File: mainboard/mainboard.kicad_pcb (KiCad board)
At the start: 2 copper layers, 344.7 x 96.3 mm, 5 parts

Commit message: grounding
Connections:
- A1 pad 100: /H2-48 -> GND
- A1 pad 61: /H2-9 -> GND
- A1 pad 66: /H2-14 -> GND
- A1 pad 69: /H2-17 -> GND
- A1 pad 73: /H2-21 -> GND
- A1 pad 74: /H2-22 -> GND
- A1 pad 81: /H2-29 -> GND
- A1 pad 82: /H2-30 -> GND
- A1 pad 84: /H2-32 -> GND
- A1 pad 99: /H2-47 -> GND
- A2 pad 100: /H2-48 -> GND
- A2 pad 61: /H2-9 -> GND
- A2 pad 66: /H2-14 -> GND
- A2 pad 69: /H2-17 -> GND
- A2 pad 73: /H2-21 -> GND
- A2 pad 74: /H2-22 -> GND
- A2 pad 81: /H2-29 -> GND
- A2 pad 82: /H2-30 -> GND
- A2 pad 84: /H2-32 -> GND
- A2 pad 99: /H2-47 -> GND
- A3 pad 100: /H2-48 -> GND
- A3 pad 61: /H2-9 -> GND
- A3 pad 66: /H2-14 -> GND
- A3 pad 69: /H2-17 -> GND
- A3 pad 73: /H2-21 -> GND
- A3 pad 74: /H2-22 -> GND
- A3 pad 81: /H2-29 -> GND
- A3 pad 82: /H2-30 -> GND
- A3 pad 84: /H2-32 -> GND
- A3 pad 99: /H2-47 -> GND
- A4 pad 100: /H2-48 -> GND
- A4 pad 61: /H2-9 -> GND
- A4 pad 66: /H2-14 -> GND
- A4 pad 69: /H2-17 -> GND
- A4 pad 73: /H2-21 -> GND
- A4 pad 74: /H2-22 -> GND
- A4 pad 81: /H2-29 -> GND
- A4 pad 82: /H2-30 -> GND
- A4 pad 84: /H2-32 -> GND
- A4 pad 99: /H2-47 -> GND
- A5 pad 100: /H2-48 -> GND
- A5 pad 61: /H2-9 -> GND
- A5 pad 66: /H2-14 -> GND
- A5 pad 69: /H2-17 -> GND
- A5 pad 73: /H2-21 -> GND
- A5 pad 74: /H2-22 -> GND
- A5 pad 81: /H2-29 -> GND
- A5 pad 82: /H2-30 -> GND
- A5 pad 84: /H2-32 -> GND
- A5 pad 99: /H2-47 -> GND
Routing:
- net GND: track 0.00 -> 159.0 mm
- net /H1-47: track 1.88 -> 86.9 mm
- net /H1-48: track 4.90 -> 87.1 mm, vias 0 -> 2
- net /H2-22: track 10.6 -> 0.00 mm
- net /H2-14: track 10.4 -> 0.00 mm
- net /H2-32: track 10.4 -> 0.00 mm
- net /H2-30: track 10.4 -> 0.00 mm
- net /H2-48: track 10.0 -> 0.00 mm
- net /H2-21: track 7.53 -> 0.00 mm
- net /H2-17: track 7.53 -> 0.00 mm
- net /H2-9: track 7.53 -> 0.00 mm
- net /H2-29: track 7.53 -> 0.00 mm
- net /H2-47: track 7.42 -> 0.00 mm

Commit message: bus power flags, finish left side routing
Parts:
- added H1: MountingHole, MountingHole:MountingHole_3.2mm_M3, F.Cu at (-58.5, 117.3)
- added H2: MountingHole, MountingHole:MountingHole_3.2mm_M3, F.Cu at (-58.5, 24.8)
- moved A2 39.6 mm to (329.0, 25.0)
- moved A1 24.4 mm to (222.0, 25.0)
- moved A3 9.55 mm to (115.0, 25.0)
- moved A5 3.68 mm to (10.4, 112.1)
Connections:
- A1 pad 100: GND -> /H2-48
- A1 pad 61: GND -> /H2-9
- A1 pad 66: GND -> /H2-14
- A1 pad 69: GND -> /H2-17
- A1 pad 73: GND -> /H2-21
- A1 pad 74: GND -> /H2-22
- A1 pad 77: /H2-25 -> +5V
- A1 pad 78: /H2-26 -> +5V
- A1 pad 79: /H2-27 -> +3V3
- A1 pad 80: /H2-28 -> +3V3
- A1 pad 97: /H2-45 -> +BATT
- A1 pad 98: /H2-46 -> +BATT
- A1 pad 99: GND -> /H2-47
- A2 pad 100: GND -> /H2-48
- A2 pad 61: GND -> /H2-9
- A2 pad 66: GND -> /H2-14
- A2 pad 69: GND -> /H2-17
- A2 pad 73: GND -> /H2-21
- A2 pad 74: GND -> /H2-22
- A2 pad 77: /H2-25 -> +5V
- A2 pad 78: /H2-26 -> +5V
- A2 pad 79: /H2-27 -> +3V3
- A2 pad 80: /H2-28 -> +3V3
- A2 pad 97: /H2-45 -> +BATT
- A2 pad 98: /H2-46 -> +BATT
- A2 pad 99: GND -> /H2-47
- A3 pad 100: GND -> /H2-48
- A3 pad 61: GND -> /H2-9
- A3 pad 66: GND -> /H2-14
- A3 pad 69: GND -> /H2-17
- A3 pad 73: GND -> /H2-21
- A3 pad 74: GND -> /H2-22
- A3 pad 77: /H2-25 -> +5V
- A3 pad 78: /H2-26 -> +5V
- A3 pad 79: /H2-27 -> +3V3
- A3 pad 80: /H2-28 -> +3V3
- A3 pad 97: /H2-45 -> +BATT
- A3 pad 98: /H2-46 -> +BATT
- A3 pad 99: GND -> /H2-47
- A4 pad 100: GND -> /H2-48
- A4 pad 61: GND -> /H2-9
- A4 pad 66: GND -> /H2-14
- A4 pad 69: GND -> /H2-17
- A4 pad 73: GND -> /H2-21
- A4 pad 74: GND -> /H2-22
- A4 pad 77: /H2-25 -> +5V
- A4 pad 78: /H2-26 -> +5V
- A4 pad 79: /H2-27 -> +3V3
- A4 pad 80: /H2-28 -> +3V3
- A4 pad 97: /H2-45 -> +BATT
- A4 pad 98: /H2-46 -> +BATT
- A4 pad 99: GND -> /H2-47
- A5 pad 100: GND -> /H2-48
- A5 pad 61: GND -> /H2-9
- A5 pad 66: GND -> /H2-14
- A5 pad 69: GND -> /H2-17
- A5 pad 73: GND -> /H2-21
- A5 pad 74: GND -> /H2-22
- A5 pad 77: /H2-25 -> +5V
- A5 pad 78: /H2-26 -> +5V
- A5 pad 79: /H2-27 -> +3V3
- A5 pad 80: /H2-28 -> +3V3
- A5 pad 97: /H2-45 -> +BATT
- A5 pad 98: /H2-46 -> +BATT
- A5 pad 99: GND -> /H2-47
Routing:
- net +BATT: track 0.00 -> 181.4 mm, vias 0 -> 4
- net +3V3: track 0.00 -> 93.3 mm, vias 0 -> 1
- net +5V: track 0.00 -> 93.2 mm, vias 0 -> 1
- net /H2-1: track 0.00 -> 90.8 mm, vias 0 -> 3
- net /H2-47: track 0.00 -> 90.8 mm, vias 0 -> 3
- net /H2-17: track 0.00 -> 90.8 mm, vias 0 -> 3
- net /H2-9: track 0.00 -> 90.8 mm, vias 0 -> 3
- net /H2-21: track 0.00 -> 90.8 mm, vias 0 -> 3
- net /H2-48: track 0.00 -> 90.7 mm, vias 0 -> 1
- net /H2-22: track 0.00 -> 90.6 mm, vias 0 -> 1
- net /H2-14: track 0.00 -> 90.6 mm, vias 0 -> 1
- net /H1-31: track 1.88 -> 90.6 mm, vias 0 -> 1
- net /H1-29: track 1.88 -> 90.5 mm, vias 0 -> 1
- net /H1-1: track 1.88 -> 90.5 mm, vias 0 -> 1
- net /H1-3: track 1.88 -> 90.5 mm, vias 0 -> 1
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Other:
- board size 344.7 x 96.3 mm -> 391.3 x 99.9 mm

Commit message: silkscreen, horizontal routing
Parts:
- added REF**: OSHW-Logo2_14.6x12mm_SilkScreen, Symbol:OSHW-Logo2_14.6x12mm_SilkScreen, F.Cu at (-44.2, 90.2)
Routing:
- net /H1-27: track 90.4 -> 396.9 mm
- net /H1-28: track 90.8 -> 397.2 mm
- net /H2-52: track 90.7 -> 396.6 mm
- net /H1-29: track 90.5 -> 396.4 mm
- net /H1-52: track 90.8 -> 396.7 mm
- net +3V3: track 93.3 -> 399.2 mm
- net GND: track 97.8 -> 403.7 mm
- net +5V: track 93.2 -> 399.0 mm
- net /H1-30: track 91.0 -> 396.9 mm
- net /H1-46: track 90.8 -> 396.6 mm
- net /H1-51: track 90.6 -> 396.2 mm
- net /H1-16: track 91.0 -> 396.5 mm
- net /H2-34: track 90.6 -> 396.1 mm
- net /H2-35: track 90.8 -> 396.2 mm
- net /H2-51: track 90.8 -> 396.2 mm
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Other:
- board text added: "PC104 Flatsat Interface Board 3 Boards, Wide bus power traces Alan Hsu v1 https://github.com/Alan-JH/Flatsat"

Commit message: finish pc104 connections
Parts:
- moved A3 0.10 mm to (115.1, 25.0)
- moved A2 0.09 mm to (328.9, 25.0)
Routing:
- net /H2-52: track 396.6 -> 642.7 mm, vias 1 -> 4
- net /H2-50: track 396.0 -> 634.8 mm, vias 1 -> 4
- net /H2-51: track 396.2 -> 629.6 mm, vias 3 -> 9
- net /H2-48: track 395.7 -> 626.0 mm, vias 1 -> 4
- net /H1-52: track 396.7 -> 625.8 mm, vias 3 -> 9
- net /H2-49: track 395.6 -> 620.8 mm, vias 3 -> 9
- net /H1-50: track 396.1 -> 617.8 mm, vias 3 -> 9
- net +BATT: track 398.6 -> 617.9 mm, vias 1 -> 4
- net /H1-51: track 396.2 -> 614.3 mm, vias 1 -> 4
- net /H2-47: track 396.1 -> 610.6 mm, vias 3 -> 9
- net /H1-48: track 395.8 -> 608.3 mm, vias 3 -> 9
- net /H2-44: track 395.5 -> 607.0 mm, vias 1 -> 4
- net /H1-49: track 395.7 -> 605.9 mm, vias 1 -> 4
- net /H2-42: track 394.7 -> 598.3 mm, vias 1 -> 4
- net /H1-46: track 396.6 -> 597.8 mm, vias 3 -> 9
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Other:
- board text added: "PC104"

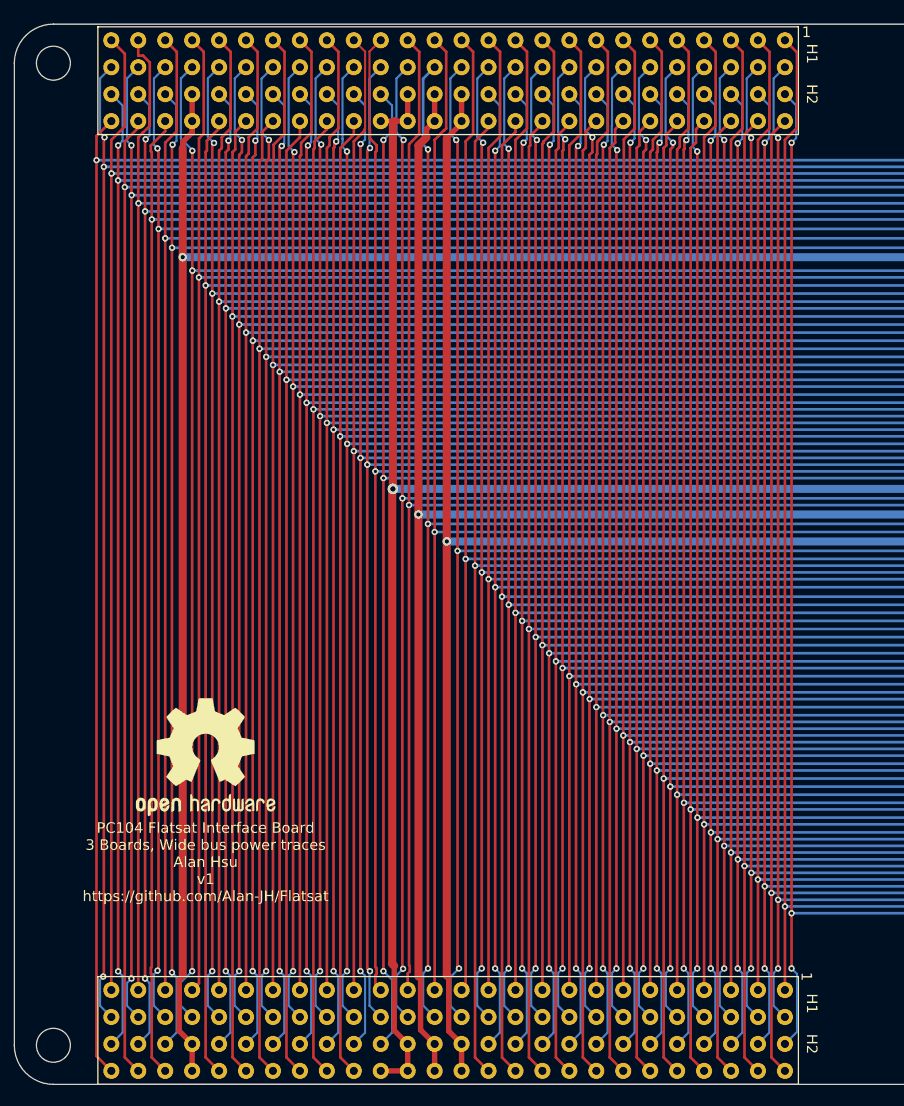
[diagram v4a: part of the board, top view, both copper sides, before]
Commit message: adapt bridge and breakout to jlcpcb tolerance, add pin numbers to mainboard
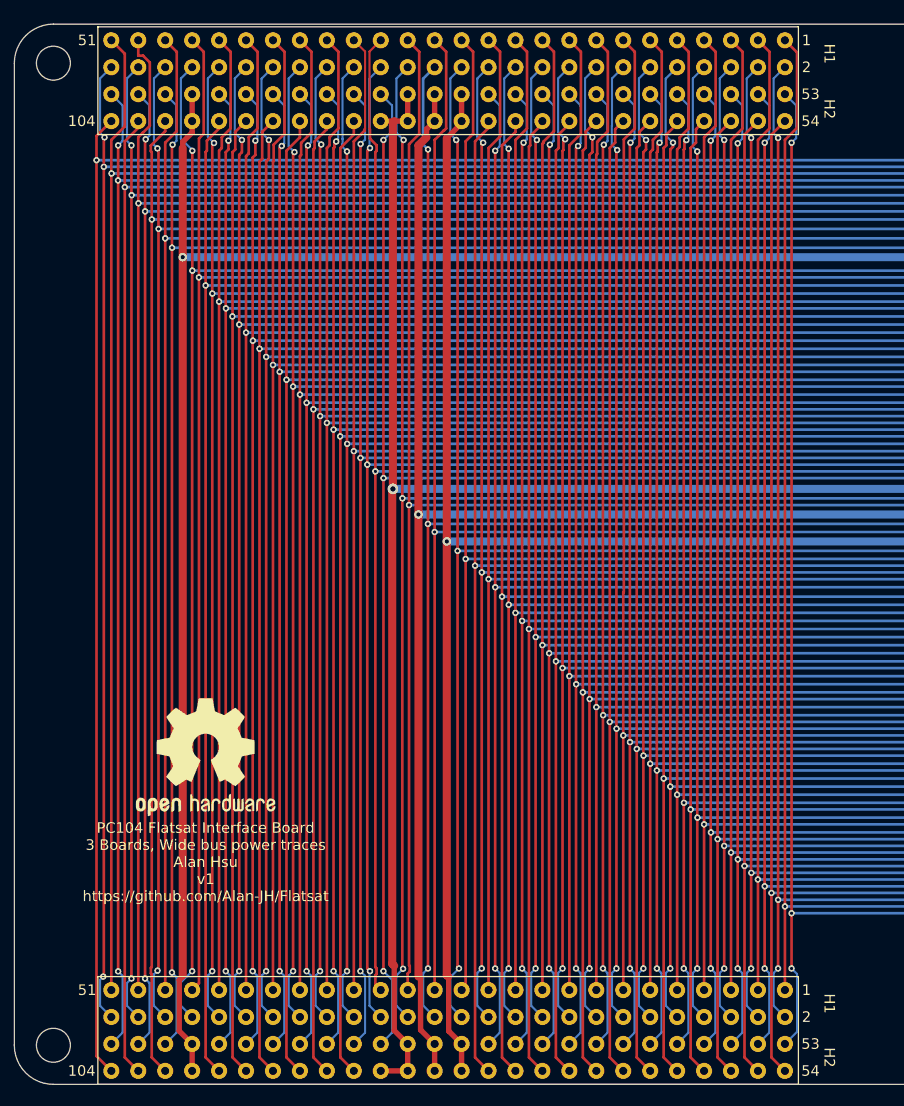
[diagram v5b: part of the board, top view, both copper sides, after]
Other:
- board text added: "104"
- board text added: "2"
- board text added: "51"
- board text added: "53"
- board text added: "54"
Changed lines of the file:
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@@
       (effects (font (size 1 1) (thickness 0.15)))
     )
-    (fp_text user "H1" (at 1.27 -2.54 -90 unlocked) (layer "F.SilkS")
-      (effects (font (size 1 1) (thickness 0.15)))
-    )
-    (fp_text user "H2" (at 5.08 -2.54 -90 unlocked) (layer "F.SilkS")
-      (effects (font (size 1 1) (thickness 0.15)))
-    )
-    (fp_text user "1" (at -0.762 -2.032 unlocked) (layer "F.SilkS")
+    (fp_text user "H1" (at 1.27 -4.191 -90 unlocked) (layer "F.SilkS")
+      (effects (font (size 1 1) (thickness 0.15)))
+    )
+    (fp_text user "H2" (at 6.477 -4.191 -90 unlocked) (layer "F.SilkS")
+      (effects (font (size 1 1) (thickness 0.15)))
+    )
+    (fp_text user "1" (at 0 -2.032 unlocked) (layer "F.SilkS")
       (effects (font (size 1 1) (thickness 0.15)))
     )
@@
       (effects (font (size 1 1) (thickness 0.15)))
     )
-    (fp_text user "1" (at -1.27 -2.032 -90 unlocked) (layer "F.SilkS")
-      (effects (font (size 1 1) (thickness 0.15)))
-    )
-    (fp_text user "H1" (at 1.27 -2.54 -90 unlocked) (layer "F.SilkS")
-      (effects (font (size 1 1) (thickness 0.15)))
-    )
-    (fp_text user "H2" (at 5.08 -2.54 -90 unlocked) (layer "F.SilkS")
+    (fp_text user "1" (at 0 -2.032 unlocked) (layer "F.SilkS")
+      (effects (font (size 1 1) (thickness 0.15)))
+    )
+    (fp_text user "H1" (at 1.27 -4.191 -90 unlocked) (layer "F.SilkS")
+      (effects (font (size 1 1) (thickness 0.15)))
+    )
+    (fp_text user "H2" (at 6.35 -4.191 -90 unlocked) (layer "F.SilkS")
       (effects (font (size 1 1) (thickness 0.15)))
     )
@@
   (gr_arc (start -62.23 24.765) (mid -61.151274 22.160726) (end -58.547 21.082) (layer "Edge.Cuts") (width 0.1))
   (gr_line (start -62.23 117.348) (end -62.23 24.765) (layer "Edge.Cuts") (width 0.1))
+  (gr_text "53" (at 12.827 27.686) (layer "F.SilkS")
+    (effects (font (size 1 1) (thickness 0.15)))
+  )
+  (gr_text "51" (at -55.372 22.606) (layer "F.SilkS")
+    (effects (font (size 1 1) (thickness 0.15)))
+  )
+  (gr_text "2" (at 12.446 114.681) (layer "F.SilkS")
+    (effects (font (size 1 1) (thickness 0.15)))
+  )
+  (gr_text "2" (at 12.446 25.146) (layer "F.SilkS")
+    (effects (font (size 1 1) (thickness 0.15)))
+  )
+  (gr_text "54" (at 12.827 119.761) (layer "F.SilkS")
+    (effects (font (size 1 1) (thickness 0.15)))
+  )
+  (gr_text "104" (at -55.88 119.761) (layer "F.SilkS")
+    (effects (font (size 1 1) (thickness 0.15)))
+  )
   (gr_text "PC104 Flatsat Interface Board\n3 Boards, Wide bus power traces\nAlan Hsu\nv1\nhttps://github.com/Alan-JH/Flatsat" (at -44.196 100.076) (layer "F.SilkS")
     (effects (font (size 1 1) (thickness 0.15)))
   )
+  (gr_text "53" (at 12.827 117.221) (layer "F.SilkS")
+    (effects (font (size 1 1) (thickness 0.15)))
+  )
+  (gr_text "54" (at 12.827 30.226) (layer "F.SilkS")
+    (effects (font (size 1 1) (thickness 0.15)))
+  )
+  (gr_text "104" (at -55.88 30.226) (layer "F.SilkS")
+    (effects (font (size 1 1) (thickness 0.15)))
+  )
+  (gr_text "51" (at -55.372 112.141) (layer "F.SilkS")
+    (effects (font (size 1 1) (thickness 0.15)))
+  )

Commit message: make prettier
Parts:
- moved H1 0.25 mm to (-58.5, 117.6)
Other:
- board size 391.3 x 99.9 mm -> 393.6 x 100.2 mm
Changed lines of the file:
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@@
   )
   (footprint "MountingHole:MountingHole_3.2mm_M3" (layer "F.Cu")
-    (at -58.547 117.348)
+    (at -58.547 117.602)
     (descr "Mounting Hole 3.2mm, no annular, M3")
     (tags "mounting hole 3.2mm no annular m3")
@@
       (net 89 "/H2-52") (pinfunction "Pin_52") (pintype "passive"))
   )
-  (gr_line (start 329.057 24.765) (end 329.057 117.348) (layer "Edge.Cuts") (width 0.1))
-  (gr_line (start -58.547 21.082) (end 325.374 21.082) (layer "Edge.Cuts") (width 0.1))
-  (gr_arc (start 325.374 21.082) (mid 327.978274 22.160726) (end 329.057 24.765) (layer "Edge.Cuts") (width 0.1))
-  (gr_arc (start -58.547 121.031) (mid -61.151274 119.952274) (end -62.23 117.348) (layer "Edge.Cuts") (width 0.1))
-  (gr_arc (start 329.057 117.348) (mid 327.978274 119.952274) (end 325.374 121.031) (layer "Edge.Cuts") (width 0.1))
-  (gr_line (start 325.374 121.031) (end -58.547 121.031) (layer "Edge.Cuts") (width 0.1))
+  (gr_line (start 331.343 24.765) (end 331.343 117.602) (layer "Edge.Cuts") (width 0.1))
+  (gr_line (start -58.547 21.082) (end 327.66 21.082) (layer "Edge.Cuts") (width 0.1))
+  (gr_arc (start 327.66 21.082) (mid 330.264274 22.160726) (end 331.343 24.765) (layer "Edge.Cuts") (width 0.1))
+  (gr_arc (start -58.547 121.285) (mid -61.151274 120.206274) (end -62.23 117.602) (layer "Edge.Cuts") (width 0.1))
+  (gr_arc (start 331.343 117.602) (mid 330.264274 120.206274) (end 327.66 121.285) (layer "Edge.Cuts") (width 0.1))
+  (gr_line (start 327.66 121.285) (end -58.547 121.285) (layer "Edge.Cuts") (width 0.1))
   (gr_arc (start -62.23 24.765) (mid -61.151274 22.160726) (end -58.547 21.082) (layer "Edge.Cuts") (width 0.1))
-  (gr_line (start -62.23 117.348) (end -62.23 24.765) (layer "Edge.Cuts") (width 0.1))
+  (gr_line (start -62.23 117.602) (end -62.23 25.019) (layer "Edge.Cuts") (width 0.1))
   (gr_text "53" (at 12.827 27.686) (layer "F.SilkS")
     (effects (font (size 1 1) (thickness 0.15)))
